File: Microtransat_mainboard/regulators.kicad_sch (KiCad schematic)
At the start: 1 part

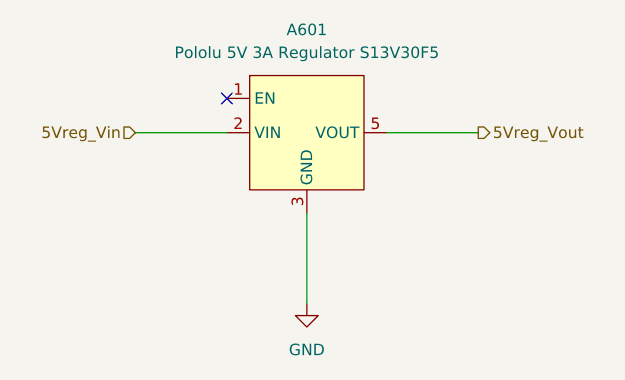
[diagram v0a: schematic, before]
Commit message: Added switch
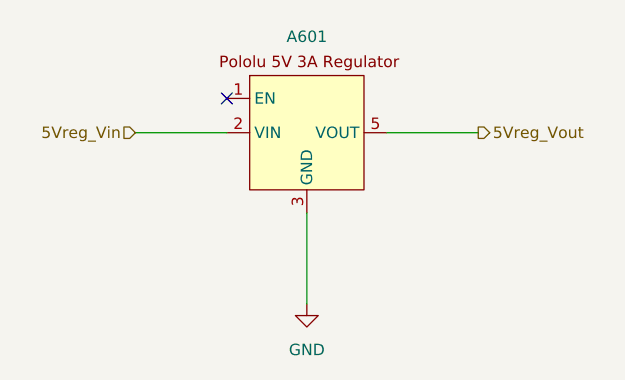
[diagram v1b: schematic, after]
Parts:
- removed A601: Pololu 5V 3A Regulator S13V30F5, Microtransat:Pololu 5V 3A Regulator, symbol GTMRG-Boards:Pololu_S13V30F5
- added A601: ~, Microtransat:Pololu 5V 3A Regulator, symbol Microtransat:Regulator
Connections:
- net 5Vreg_Vin: now also A601.2 (VIN)
- net 5Vreg_Vout: now also A601.5 (VOUT)
- net GND: now also A601.3 (GND), A601.4 (GND)
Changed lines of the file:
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@@
+	)
+	(symbol
+		(lib_id "Microtransat:Regulator")
+		(at 104.14 59.69 0)
+		(unit 1)
+		(exclude_from_sim no)
+		(in_bom yes)
+		(on_board yes)
+		(dnp no)
+		(property "Reference" "A601"
+			(at 104.14 50.292 0)
+			(effects
+				(font
+					(size 1.27 1.27)
+				)
+			)
+		)
+		(property "Value" "~"
+			(at 104.394 49.53 0)
+			(effects
+				(font
+					(size 1.27 1.27)
+				)
+				(hide yes)
+			)
+		)
+		(property "Footprint" "Microtransat:Pololu 5V 3A Regulator"
+			(at 104.14 59.69 0)
+			(effects
+				(font
+					(size 1.27 1.27)
+				)
+				(hide yes)
+			)
+		)
+		(property "Datasheet" ""
+			(at 104.14 59.69 0)
+			(effects
+				(font
+					(size 1.27 1.27)
+				)
+				(hide yes)
+			)
+		)
+		(property "Description" ""
+			(at 104.14 59.69 0)
+			(effects
+				(font
+					(size 1.27 1.27)
+				)
+				(hide yes)
+			)
+		)
+		(pin "2"
+		)
+		(pin "3"
+		)
+		(pin "4"
+		)
+		(pin "1"
+		)
+		(pin "5"
+		)
+		(instances
+			(project ""
+				(path "/89914625-be83-416e-bb0d-b792f59b4aa6/ef83c155-5d1b-4294-b885-3978818ca0db"
+					(reference "A601")
+					(unit 1)
+				)
+			)
+		)
 	)
 	(symbol
@@
 					(unit 1)
 				)
-			)
-		)
-	)
-	(symbol
-		(lib_id "GTMRG-Boards:Pololu_S13V30F5")
-		(at 104.14 60.96 0)
-		(unit 1)
-		(exclude_from_sim no)
-		(in_bom yes)
-		(on_board yes)
-		(dnp no)
-		(fields_autoplaced yes)
-		(property "Reference" "A601"
-			(at 104.14 49.53 0)
-			(effects
-				(font
-					(size 1.27 1.27)
-				)
-			)
-		)
-		(property "Value" "Pololu 5V 3A Regulator S13V30F5"
-			(at 104.14 52.07 0)
-			(effects
-				(font
-					(size 1.27 1.27)
-				)
-			)
-		)
-		(property "Footprint" "Microtransat:Pololu 5V 3A Regulator"
-			(at 104.14 60.96 0)
-			(effects
-				(font
-					(size 1.27 1.27)
-				)
-				(hide yes)
-			)
-		)
-		(property "Datasheet" "https://www.pololu.com/product/4082"
-			(at 104.14 69.342 0)
-			(effects
-				(font
-					(size 1.27 1.27)
-				)
-				(hide yes)
-			)
-		)
-		(property "Description" ""
-			(at 104.14 60.96 0)
-			(effects
-				(font
-					(size 1.27 1.27)
-				)
-				(hide yes)
-			)
-		)
-		(pin "1"
-		)
-		(pin "3"
-		)
-		(pin "4"
-		)
-		(pin "5"
-		)
-		(pin "2"
-		)
-		(instances
-			(project "Microtransat_mainboard"
-				(path "/89914625-be83-416e-bb0d-b792f59b4aa6/ef83c155-5d1b-4294-b885-3978818ca0db"
-					(reference "A601")
-					(unit 1)
-				)

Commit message: Finished silkscreen/outline changes
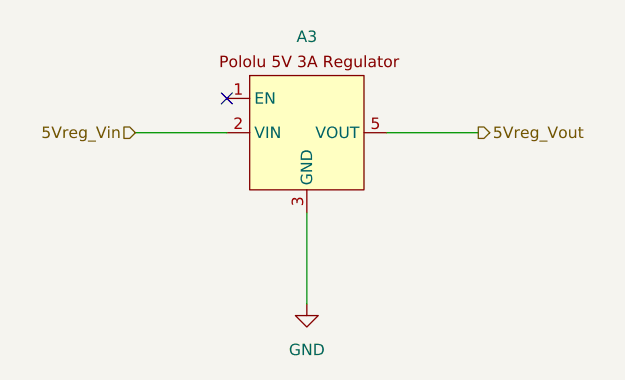
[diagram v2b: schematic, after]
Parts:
- renumbered A601 to A3
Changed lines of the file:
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@@
 		(on_board yes)
 		(dnp no)
-		(property "Reference" "A601"
+		(property "Reference" "A3"
 			(at 104.14 50.292 0)
 			(effects
@@
 			(project ""
 				(path "/89914625-be83-416e-bb0d-b792f59b4aa6/ef83c155-5d1b-4294-b885-3978818ca0db"
-					(reference "A601")
+					(reference "A3")
 					(unit 1)
 				)
@@
 		(dnp no)
 		(fields_autoplaced yes)
-		(property "Reference" "#PWR0601"
+		(property "Reference" "#PWR048"
 			(at 104.14 86.36 0)
 			(effects
@@
 			(project "Microtransat_mainboard"
 				(path "/89914625-be83-416e-bb0d-b792f59b4aa6/ef83c155-5d1b-4294-b885-3978818ca0db"
-					(reference "#PWR0601")
+					(reference "#PWR048")
 					(unit 1)
 				)

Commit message: Some small changes to silkscreen and component numbers
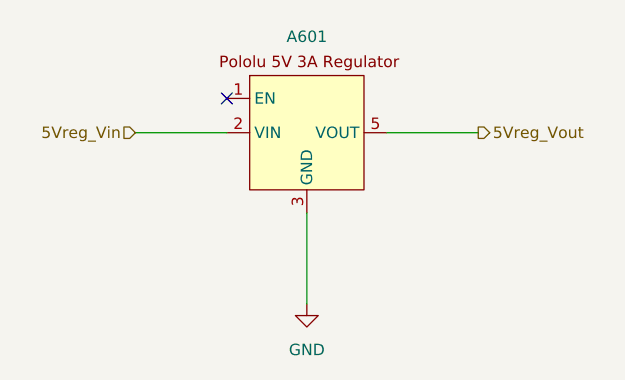
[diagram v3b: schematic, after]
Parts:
- renumbered A3 to A601
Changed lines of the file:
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@@
 		(on_board yes)
 		(dnp no)
-		(property "Reference" "A3"
+		(property "Reference" "A601"
 			(at 104.14 50.292 0)
 			(effects
@@
 			(project ""
 				(path "/89914625-be83-416e-bb0d-b792f59b4aa6/ef83c155-5d1b-4294-b885-3978818ca0db"
-					(reference "A3")
+					(reference "A601")
 					(unit 1)
 				)
@@
 		(dnp no)
 		(fields_autoplaced yes)
-		(property "Reference" "#PWR048"
+		(property "Reference" "#PWR0601"
 			(at 104.14 86.36 0)
 			(effects
@@
 			(project "Microtransat_mainboard"
 				(path "/89914625-be83-416e-bb0d-b792f59b4aa6/ef83c155-5d1b-4294-b885-3978818ca0db"
-					(reference "#PWR048")
+					(reference "#PWR0601")
 					(unit 1)
 				)
